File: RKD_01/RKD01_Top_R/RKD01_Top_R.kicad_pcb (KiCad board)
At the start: 2 copper layers, 197.6 x 102.4 mm, 50 parts, among them SW36 SW_Push, SW37 SW_Push, SW38 SW_Push, SW39 SW_Push, SW40 SW_Push, SW41 SW_Push, SW42 SW_Push, SW43 SW_Push, SW44 SW_Push, SW45 SW_Push, SW46 SW_Push, SW47 SW_Push, SW48 SW_Push, SW49 SW_Push, SW50 SW_Push, SW51 SW_Push, SW52 SW_Push, SW53 SW_Push, SW54 SW_Push, SW55 SW_Push, SW56 SW_Push, SW57 SW_Push, SW58 SW_Push, SW59 SW_Push, SW60 SW_Push, SW61 SW_Push, SW62 SW_Push, SW63 SW_Push, SW64 SW_Push, SW65 SW_Push, SW66 SW_PUSH, SW66 SW_Push, SW67 SW_Push, SW68 SW_Push, SW69 SW_Push, SW70 SW_Push, SW71 SW_Push, SW72 SW_Push, SW73 SW_Push, SW74 SW_Push, SW75 SW_Push, SW76 SW_Push

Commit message: 構成変更
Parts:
- removed the SW66 at (190.5, 57.1)
- removed the SW66 at (188.1, 95.2)
- added Ref**: Val**, kbd_Hole:m2_Screw_Hole, F.Cu at (147.6, 23.8)
- added Ref**: Val**, kbd_Hole:m2_Screw_Hole, F.Cu at (21.4, 23.8)
- added SW**: SW_PUSH, kbd_SW_Hole:Stab_Hole_Choc_2u_Top, F.Cu at (188.1, 95.2)
- added SW**: SW_PUSH, kbd_SW_Hole:Stab_Hole_Choc_2u_Top, F.Cu at (190.5, 57.1)
- SW39, SW74: footprint kbd_SW_Hole:SW_Hole_1u -> kbd_SW_Hole:SW_Hole_1.5u
- SW48, SW53: footprint kbd_SW_Hole:SW_Hole_1u -> kbd_SW_Hole:SW_Hole_1.25u
- moved Ref** 47.6 mm to (71.4, 47.6)
- moved Ref** 2.38 mm to (21.4, 140.5)
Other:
- board size 197.6 x 102.4 mm -> 197.6 x 126.2 mm

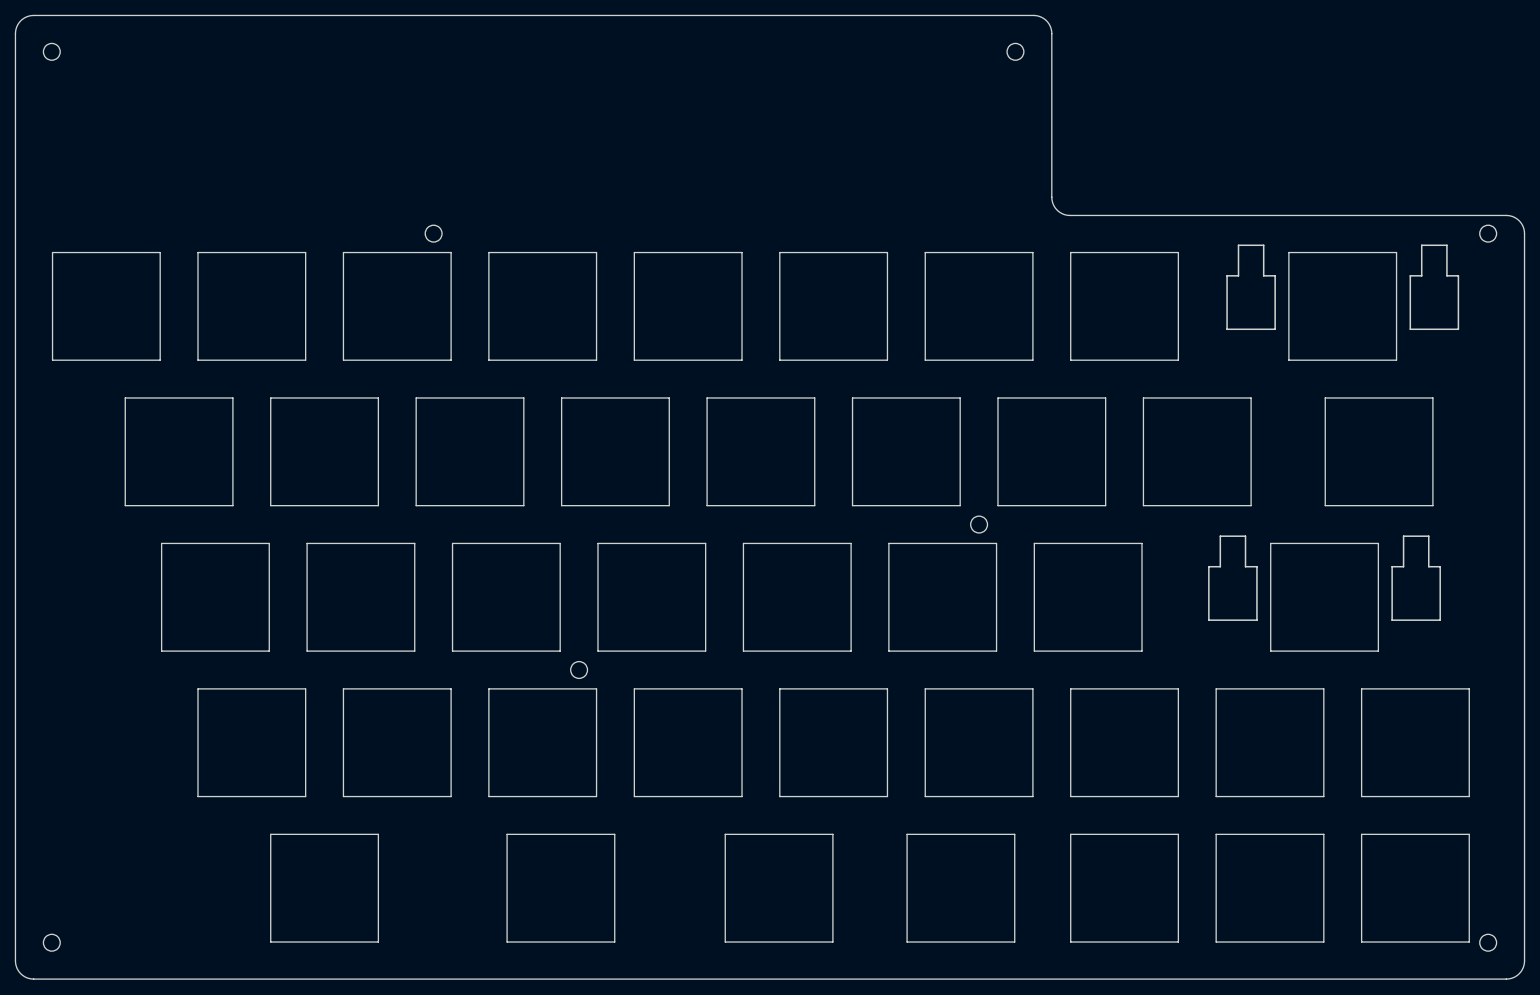
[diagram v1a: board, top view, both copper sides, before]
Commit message: 右手Top 穴の位置間違いを修正
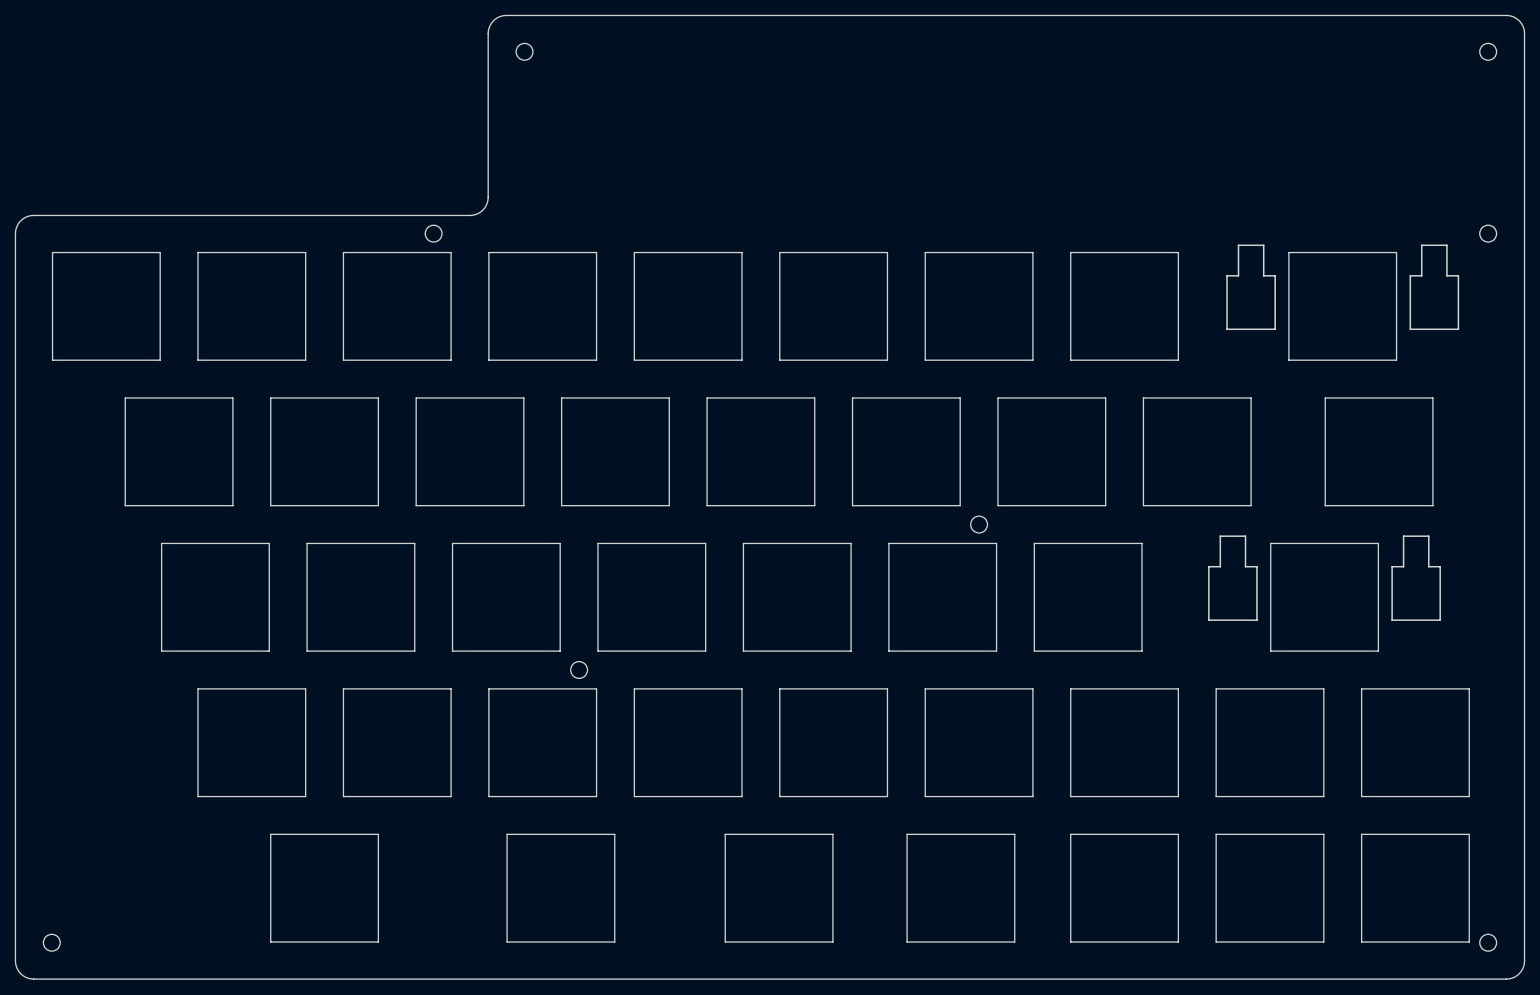
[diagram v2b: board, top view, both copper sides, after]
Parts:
- M1, M2, M3, M4, M5, M6, M7, M8: renamed from Ref**; value Val** -> Mark
- SW48: footprint kbd_SW_Hole:SW_Hole_1.25u -> kbd_SW_Hole:SW_Hole_1.75u
- SW62: footprint kbd_SW_Hole:SW_Hole_1u -> kbd_SW_Hole:SW_Hole_1.25u
- SW74: footprint kbd_SW_Hole:SW_Hole_1.5u -> kbd_SW_Hole:SW_Hole_1u
- moved M2 61.9 mm to (209.6, 23.8)
- moved M1 61.9 mm to (83.3, 23.8)
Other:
- outline, holes or cut-outs redrawn
